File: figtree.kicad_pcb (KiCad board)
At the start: 2 copper layers, 26.7 x 18.9 mm, 13 parts, among them Q1 SI2307, U1 LC_TP4056, U2 TP4054, U3 ME6211

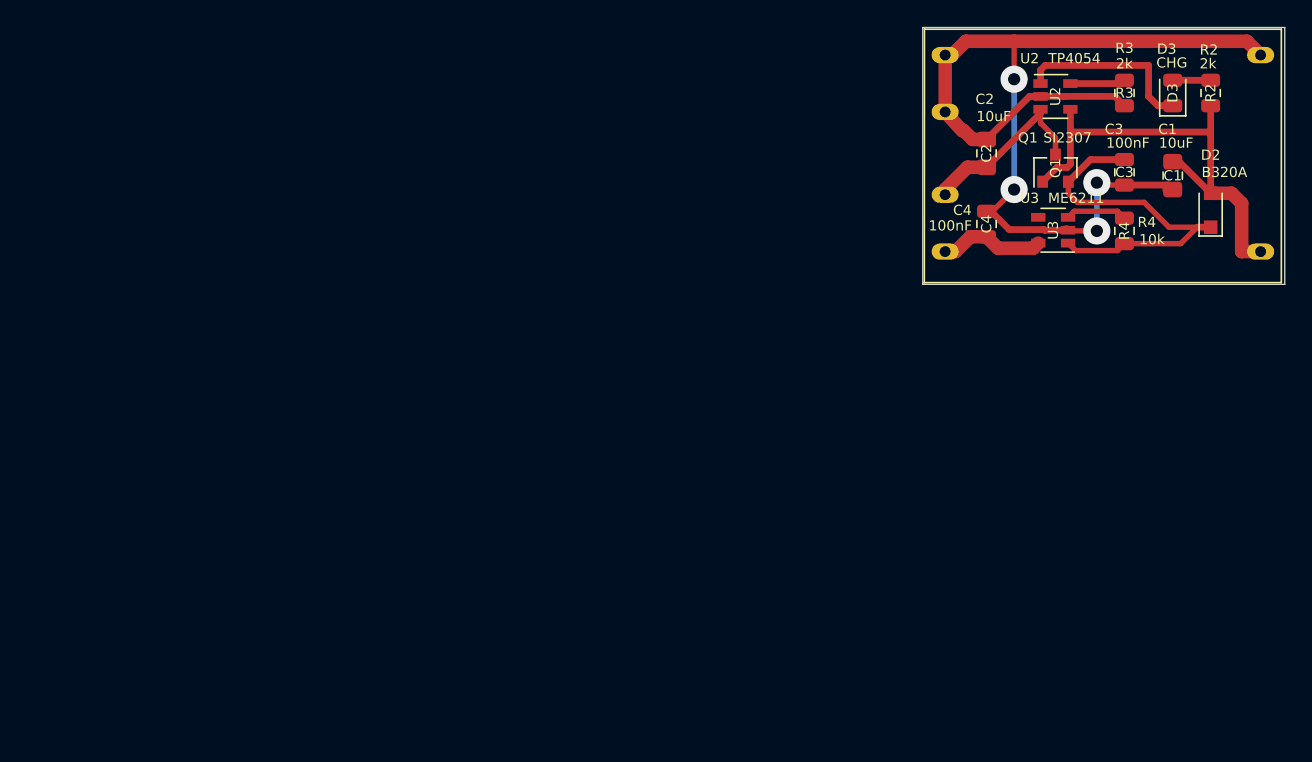
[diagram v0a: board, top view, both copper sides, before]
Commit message: Update PCB for rename
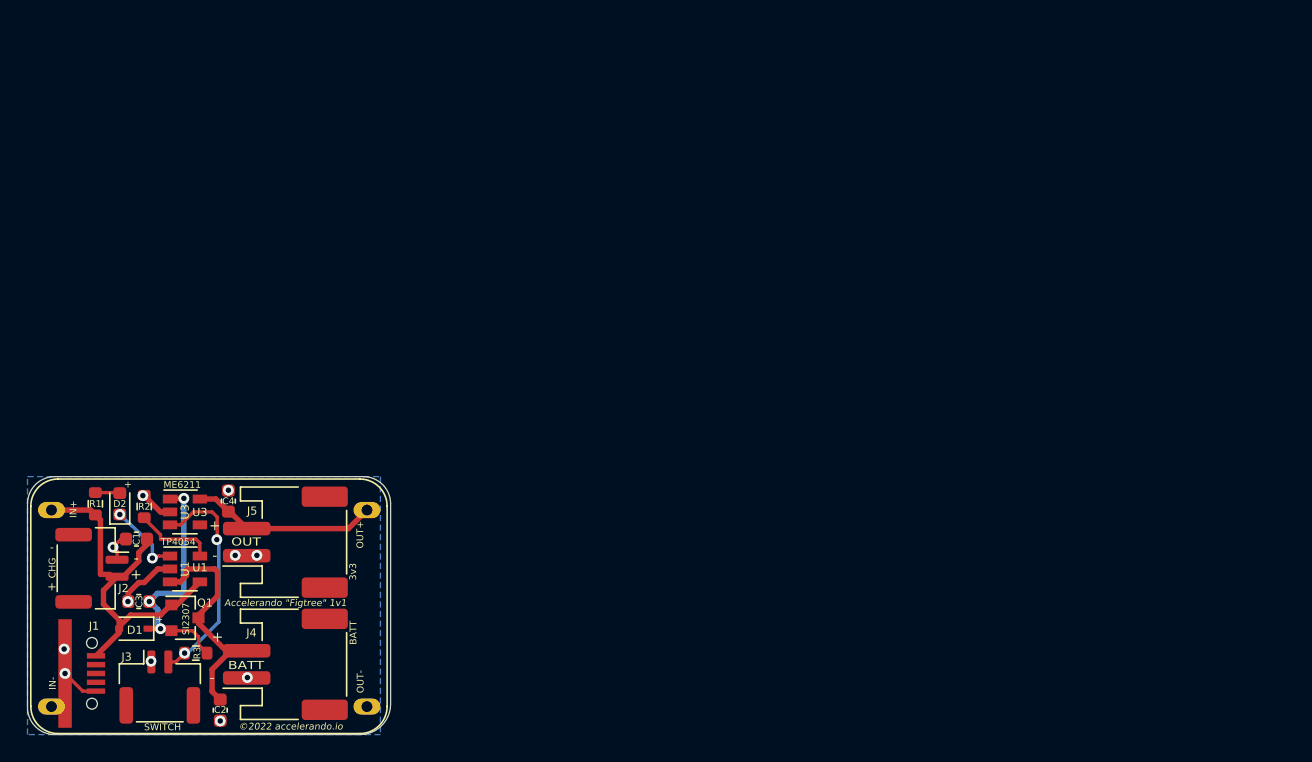
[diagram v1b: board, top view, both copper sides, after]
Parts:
- removed the U1 at (142.4, 76.7)
- added J1: USB_B_Micro, Accelerando:USB_Micro_SMD, F.Cu at (51.8, 105.5)
- added J2: CHG, Connector_JST:JST_GH_SM02B-GHS-TB_1x02-1MP_P1.25mm_Horizontal, F.Cu at (54.8, 97.8)
- added J3: Off, Connector_JST:JST_GH_SM02B-GHS-TB_1x02-1MP_P1.25mm_Horizontal, F.Cu at (59.8, 106.5)
- added J4: Batt, Connector_JST:JST_PH_S2B-PH-SM4-TB_1x02-1MP_P2.00mm_Horizontal, F.Cu at (69.0, 104.8)
- added J5: OUT, Connector_JST:JST_PH_S2B-PH-SM4-TB_1x02-1MP_P2.00mm_Horizontal, F.Cu at (69.0, 95.8)
- added U2: BUCKBOOST, Accelerando:BUCKBOOST, F.Cu at (50.2, 91.2)
- C1, C2: footprint Capacitor_SMD:C_0805_2012Metric_Pad1.15x1.40mm_HandSolder -> Capacitor_SMD:C_0603_1608Metric
- C3, C4: footprint Capacitor_SMD:C_0805_2012Metric -> Capacitor_SMD:C_0603_1608Metric
- D1: renamed from D2; footprint Diode_SMD:D_SOD-323_HandSoldering -> Diode_SMD:D_SOD-323
- D2: renamed from D3; value CHG -> LED 0603 RED; footprint LED_SMD:LED_0805_2012Metric -> LED_SMD:LED_0603_1608Metric
- R1: renamed from R2; footprint Resistor_SMD:R_0805_2012Metric -> Resistor_SMD:R_0603_1608Metric
- R2: renamed from R3; footprint Resistor_SMD:R_0805_2012Metric -> Resistor_SMD:R_0603_1608Metric
- R3: renamed from R4; footprint Resistor_SMD:R_0805_2012Metric -> Resistor_SMD:R_0603_1608Metric
- moved R1 87.6 mm to (55.0, 93.0)
- moved D1 85.1 mm to (57.8, 102.2), turned to 180 degrees
- moved D2 83.3 mm to (56.8, 93.0)
- moved C1 80.9 mm to (58.0, 95.6), turned to 180 degrees
- moved C3 79.2 mm to (58.2, 100.2), turned to 180 degrees
- moved R2 78.4 mm to (58.6, 93.2), turned to 90 degrees
- moved R3 75.1 mm to (62.4, 104.0), turned to 0 degrees
- moved U1 73.0 mm to (61.6, 97.8)
- moved Q1 72.2 mm to (61.6, 101.4), turned to 0 degrees
- moved C2 69.8 mm to (64.2, 108.2), turned to -90 degrees
- moved U3 67.2 mm to (61.6, 93.6), turned to 0 degrees
- moved C4 59.5 mm to (64.8, 92.8)
- renumbered U2 to U1
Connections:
- U3 pad 4: Net-(U3-Pad4) -> unconnected-(U3-Pad4)
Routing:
- net GND: track 76.7 -> 11.9 mm, vias 4 -> 11
- net /CE: track 4.55 -> 16.8 mm, vias 0 -> 2
- net /5v: track 27.8 -> 18.5 mm, vias 0 -> 3
- net /VIN: track 35.2 -> 27.4 mm
- net /CHRG: track 13.4 -> 5.86 mm, vias 0 -> 2
- net /VOUT: track 7.81 -> 13.7 mm
- net +BATT: track 13.9 -> 17.4 mm
- net /PROG: track 4.32 -> 5.99 mm
- net /D3+: track 2.79 -> 1.76 mm
- added copper zone on B.Cu, net GND
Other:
- board size 26.7 x 18.9 mm -> 26.8 x 19 mm
- net class Default removed
- board text added: "+"
- board text added: "-"
- board text added: "3v3"
- board text added: "Accelerando {dblquote}Figtree{dblquote} 1v1"
- board text added: "BATT"
- board text added: "CHG"
- board text added: "IN+"
- board text added: "IN-"
- board text added: "OUT"
- board text added: "OUT+"
- board text added: "OUT-"
- board text added: "SWITCH"
- board text added: "©2022 accelerando.io"
